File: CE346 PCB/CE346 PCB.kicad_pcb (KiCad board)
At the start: 2 copper layers, 54 parts, among them IC1 nRF52833-QDAA-R, J1 Conn_02x04_Odd_Even, J11 Conn_01x06_Pin, J14 Conn_01x05_Pin, J15 Conn_01x04_Pin, J16 Conn_01x04_Pin, J17 Conn_01x04_Pin, J18 Conn_01x04_Pin, J3 Conn_02x04_Odd_Even, J4 Conn_01x02_Pin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

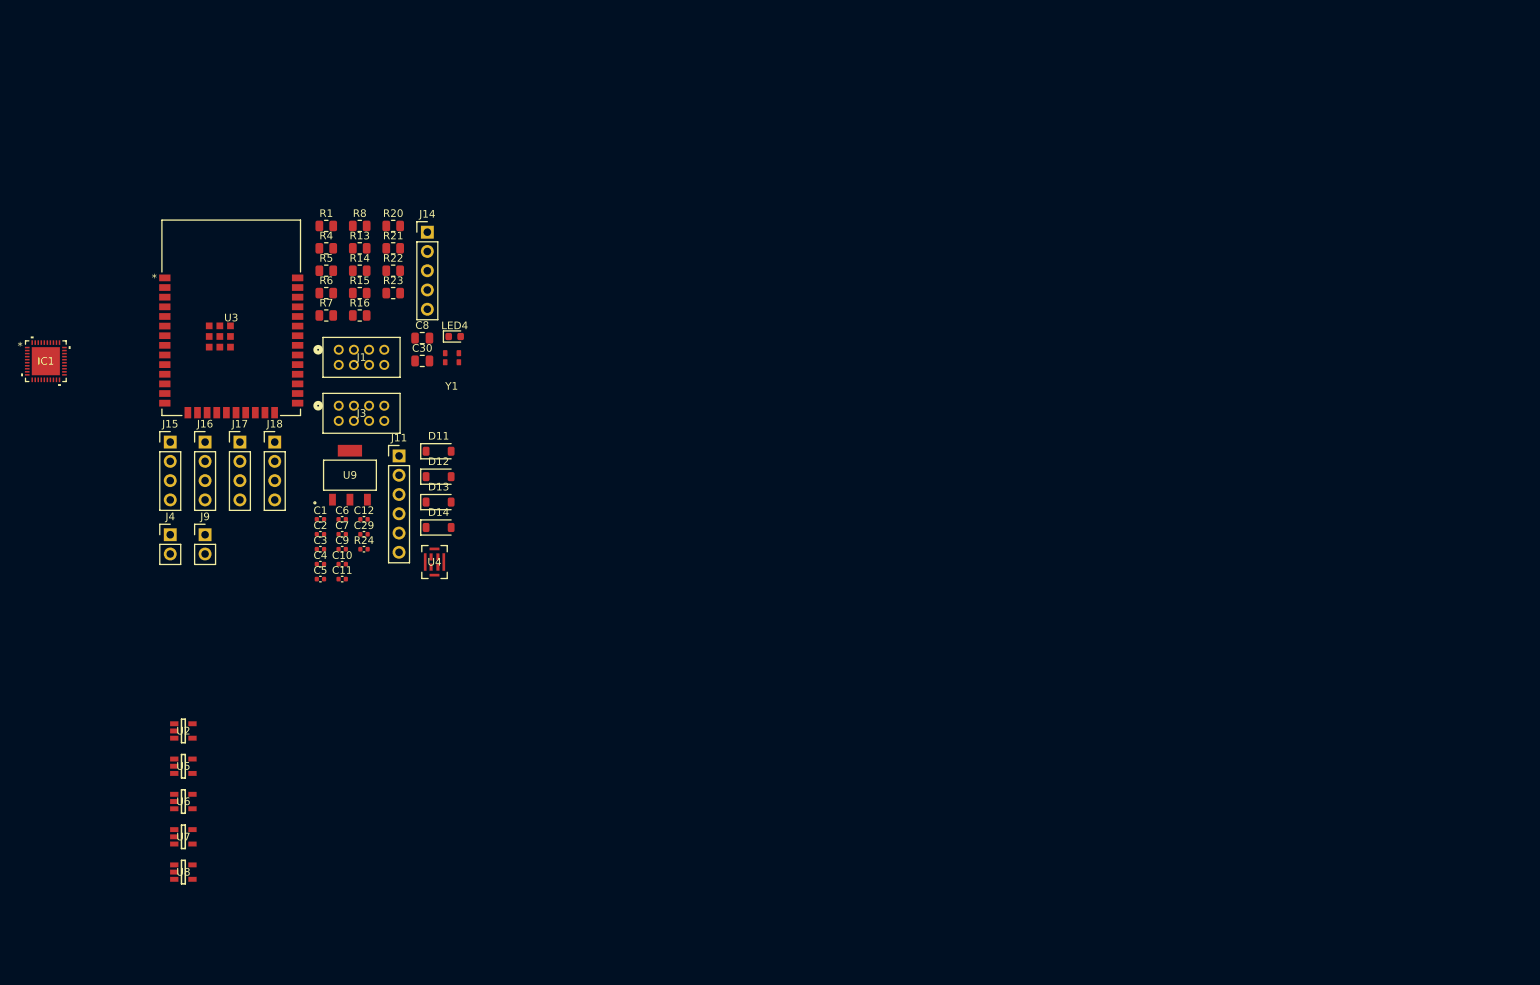
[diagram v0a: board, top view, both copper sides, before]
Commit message: pushing the changes to the routed  PCB
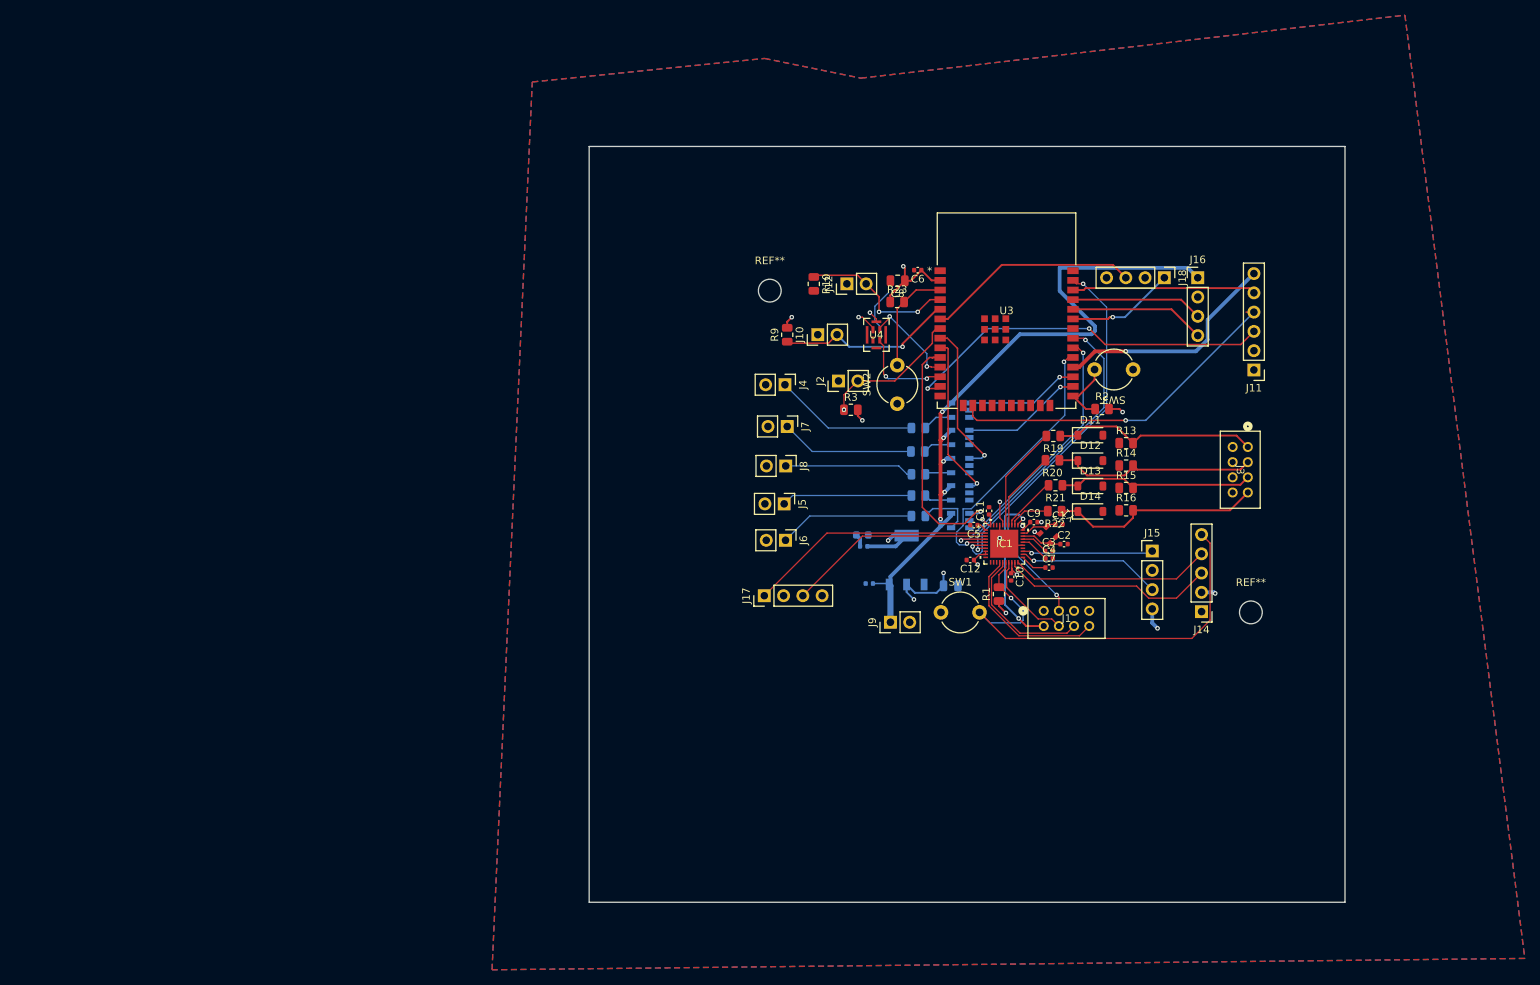
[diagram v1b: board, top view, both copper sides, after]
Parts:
- added J10: Conn_01x02_Socket, Connector_PinHeader_2.54mm:PinHeader_1x02_P2.54mm_Vertical, F.Cu at (157.4, 75.5)
- added J12: Conn_01x02_Socket, Connector_PinHeader_2.54mm:PinHeader_1x02_P2.54mm_Vertical, F.Cu at (161.3, 68.8)
- added J2: Conn_01x02_Socket, Connector_PinHeader_2.54mm:PinHeader_1x02_P2.54mm_Vertical, F.Cu at (160.2, 81.6)
- added J5: Conn_01x02_Pin, Connector_PinHeader_2.54mm:PinHeader_1x02_P2.54mm_Vertical, F.Cu at (153.0, 97.8)
- added J6: Conn_01x02_Pin, Connector_PinHeader_2.54mm:PinHeader_1x02_P2.54mm_Vertical, F.Cu at (153.2, 102.6)
- added J7: Conn_01x02_Pin, Connector_PinHeader_2.54mm:PinHeader_1x02_P2.54mm_Vertical, F.Cu at (153.4, 87.6)
- added J8: Conn_01x02_Pin, Connector_PinHeader_2.54mm:PinHeader_1x02_P2.54mm_Vertical, F.Cu at (153.2, 92.8)
- added R10: 10k, Resistor_SMD:R_0805_2012Metric, F.Cu at (156.9, 68.8)
- added R19: 330, Resistor_SMD:R_0805_2012Metric, F.Cu at (188.5, 88.8)
- added R2: 10k, Resistor_SMD:R_0805_2012Metric, F.Cu at (194.9, 85.3)
- added R3: 10k, Resistor_SMD:R_0805_2012Metric, F.Cu at (161.8, 85.4)
- added R9: 10k, Resistor_SMD:R_0805_2012Metric, F.Cu at (153.4, 75.5)
- added REF**: MountingHole_3mm, MountingHole:MountingHole_3mm, F.Cu at (151.1, 69.7)
- added REF**: MountingHole_3mm, MountingHole:MountingHole_3mm, F.Cu at (214.5, 112.1)
- added SW1: SW_Push, CE346 Footprints:pushbutton, F.Cu at (176.2, 112.1)
- added SW2: SW_Push, CE346 Footprints:pushbutton, F.Cu at (167.9, 82.1)
- added SW3: SW_Push, CE346 Footprints:pushbutton, F.Cu at (196.4, 80.1)
- C29, C30, LED4, R24, R4, R5, R6, R7, R8, U2, U5, U6, U7, U8: moved to B.Cu
- U9: footprint ldl117:SOT223_STM -> CE346 Footprints:SOT223_STM; moved to B.Cu
- moved J16 132.6 mm to (207.5, 68.0)
- moved J15 130.2 mm to (201.5, 104.0)
- moved IC1 128.6 mm to (182.0, 103.1)
- moved J3 119.9 mm to (214.1, 90.3), turned to -90 degrees
- moved J18 119.2 mm to (203.1, 68.0), turned to -90 degrees
- moved J14 113.6 mm to (208.0, 112.0), turned to 180 degrees
- moved J11 113.2 mm to (214.9, 80.2), turned to 180 degrees
- moved U8 112.4 mm to (176.2, 100.0), turned to 180 degrees
- moved U7 112.0 mm to (176.2, 96.4), turned to 180 degrees
- moved U6 111.5 mm to (176.2, 92.8), turned to 180 degrees
- moved U5 111.2 mm to (176.2, 89.1), turned to 180 degrees
- moved U2 110.8 mm to (176.2, 85.5), turned to 180 degrees
- moved R13 104.2 mm to (198.1, 89.8)
- moved R14 104.2 mm to (198.1, 92.8)
- moved R15 104.2 mm to (198.1, 95.7)
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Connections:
- IC1 pad 14: /IR_MUX_CTRL0 -> /IR_MUX_CTRL_0
- IC1 pad 15: /IR_MUX_CTRL1 -> /IR_MUX_CTRL_1
- IC1 pad 17: /IR_MUX_CTRL2 -> /IR_MUX_CTRL_2
- IC1 pad 20: /SWDCLK -> /SWCLK
- IC1 pad 31: /IR_MUX_CTRL3 -> /IR_MUX_CTRL_3
- IC1 pad 38: /DEC4/6 -> /DEC 4/6
- IC1 pad 5: /NRF_CS -> /SPI_CS
- J18 pad 3: /UART1_RX -> /UART2_RX
- U3 pad 25: unconnected-(U3-IO0-Pad25) -> Net-(U3-IO0)
- U3 pad 29: /ESP_CS -> /SPI_CS
- U3 pad 4: unconnected-(U3-SENSOR_VP-Pad4) -> /KILL_SWITCH
- U3 pad 5: unconnected-(U3-SENSOR_VN-Pad5) -> /sound_reactive_button
- U3 pad 7: unconnected-(U3-IO35-Pad7) -> /game_state_button
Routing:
- net /VDD5V0: track 0.00 -> 99.2 mm, vias 0 -> 5
- net /NRST: track 0.00 -> 60.4 mm, vias 0 -> 1
- net /VDD3V3: track 0.00 -> 50.1 mm, vias 0 -> 13
- net /BCLK: track 0.00 -> 49.6 mm, vias 0 -> 2
- net /SPI_MISO: track 0.00 -> 48.8 mm, vias 0 -> 2
- net /LRCL: track 0.00 -> 45.6 mm, vias 0 -> 1
- net /SPI_MOSI: track 0.00 -> 38.4 mm, vias 0 -> 2
- net /SPI_SCK: track 0.00 -> 36.8 mm, vias 0 -> 2
- net /SPI_CS: track 0.00 -> 35.9 mm, vias 0 -> 2
- net /DIN5: track 0.00 -> 34.0 mm, vias 0 -> 1
- net /NRF_TX: track 0.00 -> 32.6 mm
- net /SEL: track 0.00 -> 30.5 mm, vias 0 -> 1
- net /SWDIO: track 0.00 -> 28.3 mm
- net /UART2_RX: track 0.00 -> 28.1 mm
- net /PIEZO_4+: track 0.00 -> 27.8 mm
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- added copper zone on In2.Cu, net /VDD3V3
- added copper zone on B.Cu, net GND
- added copper zone on F.Cu, net GND
- added copper zone on In1.Cu, net GND
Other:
- board outline added: 99.6 x 99.6 mm
- copper layers 2 -> 4
